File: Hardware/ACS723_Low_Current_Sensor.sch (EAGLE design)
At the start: 26 parts, among them U1 ACS723, U2 OPA344

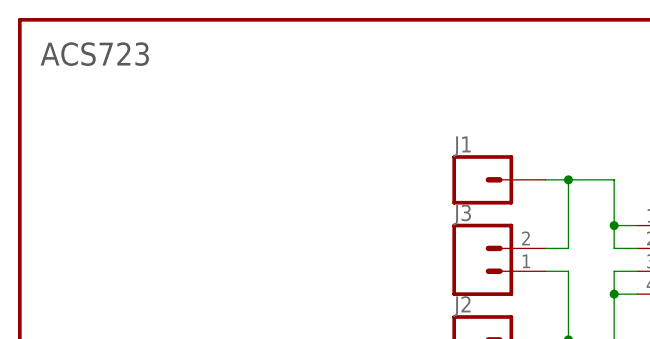
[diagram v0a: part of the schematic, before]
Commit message: SCH changes
-added full IC name
-moved some notes around
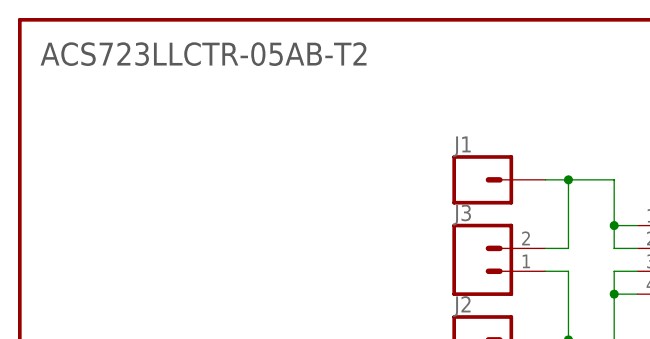
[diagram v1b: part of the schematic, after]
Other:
- note added: "ACS723LLCTR-05AB-T2"
- note removed: "ACS723"
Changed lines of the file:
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@@
 clockwise to increase
 output reference voltage</text>
-<text x="2.286" y="180.34" size="2.54" layer="97">ACS723</text>
+<text x="2.286" y="180.34" size="2.54" layer="97">ACS723LLCTR-05AB-T2</text>
 </plain>
 <instances>

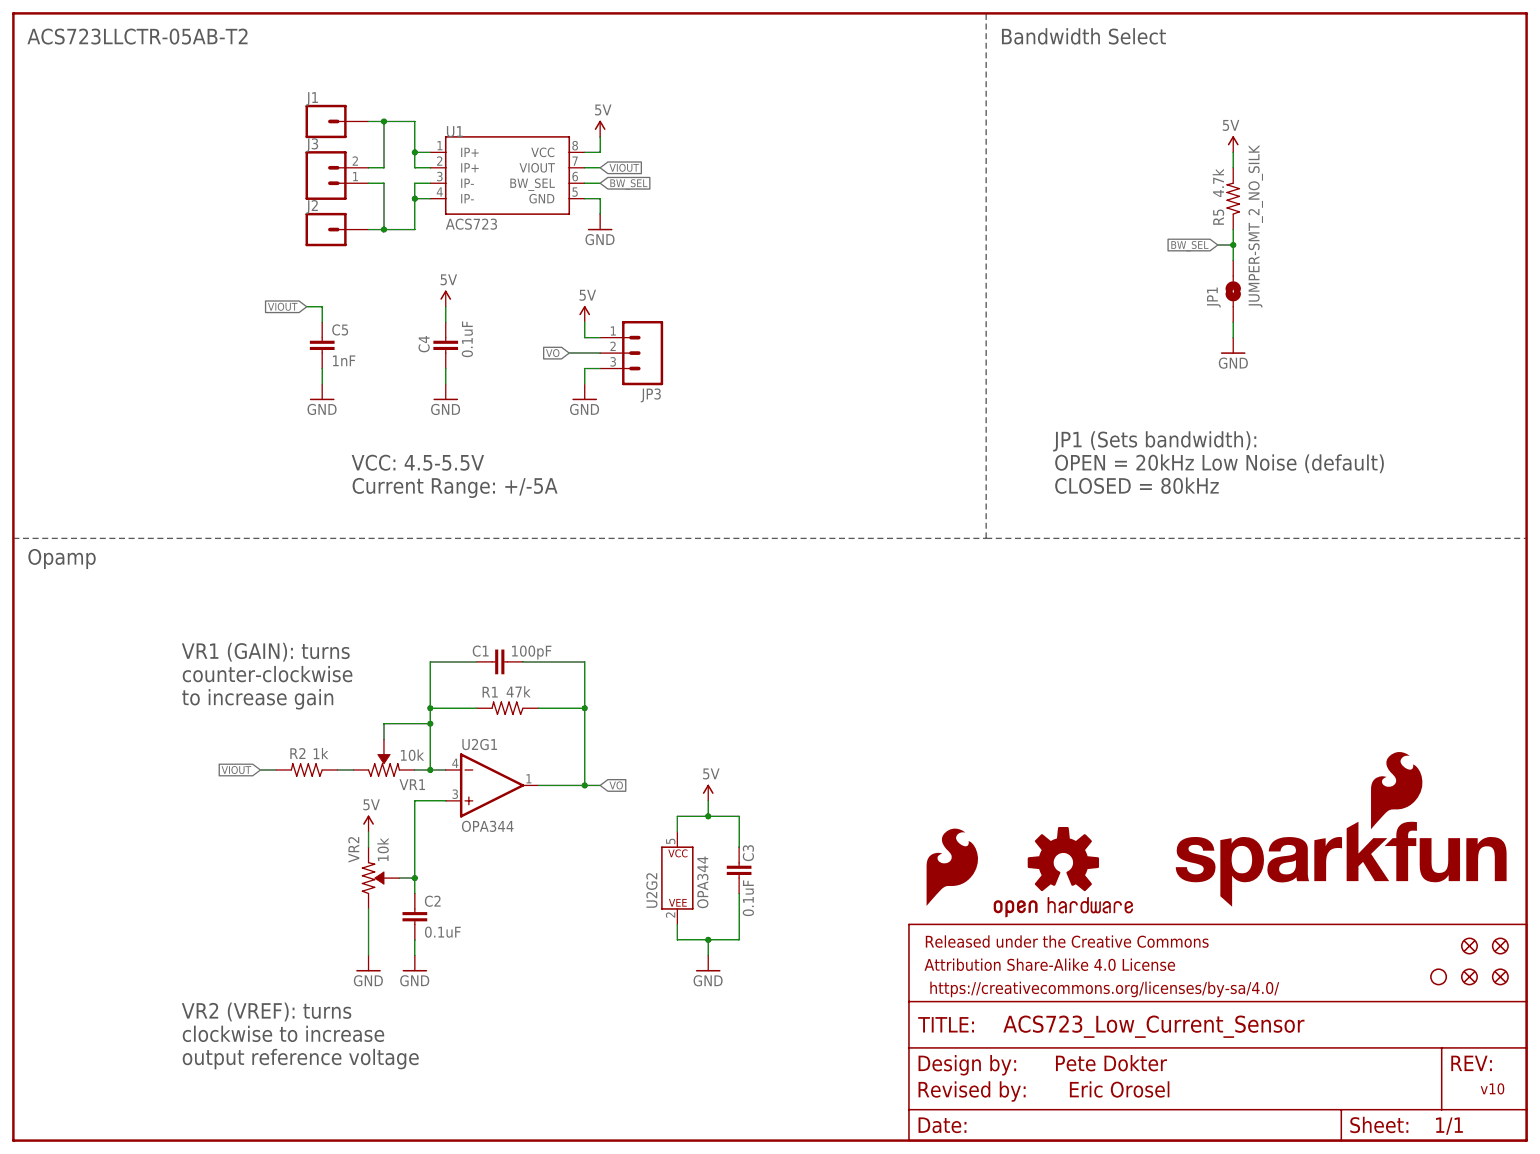
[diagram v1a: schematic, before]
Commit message: v10 finalization
-moved some vias for better GND stitching
-slight silk adjustment
-changed value of opamp voltage split to allow for similiar spectrum measurment as the previous version. With an output of 220mV more per amp the values of the gain resistors needed to be adjusted to account for this difference
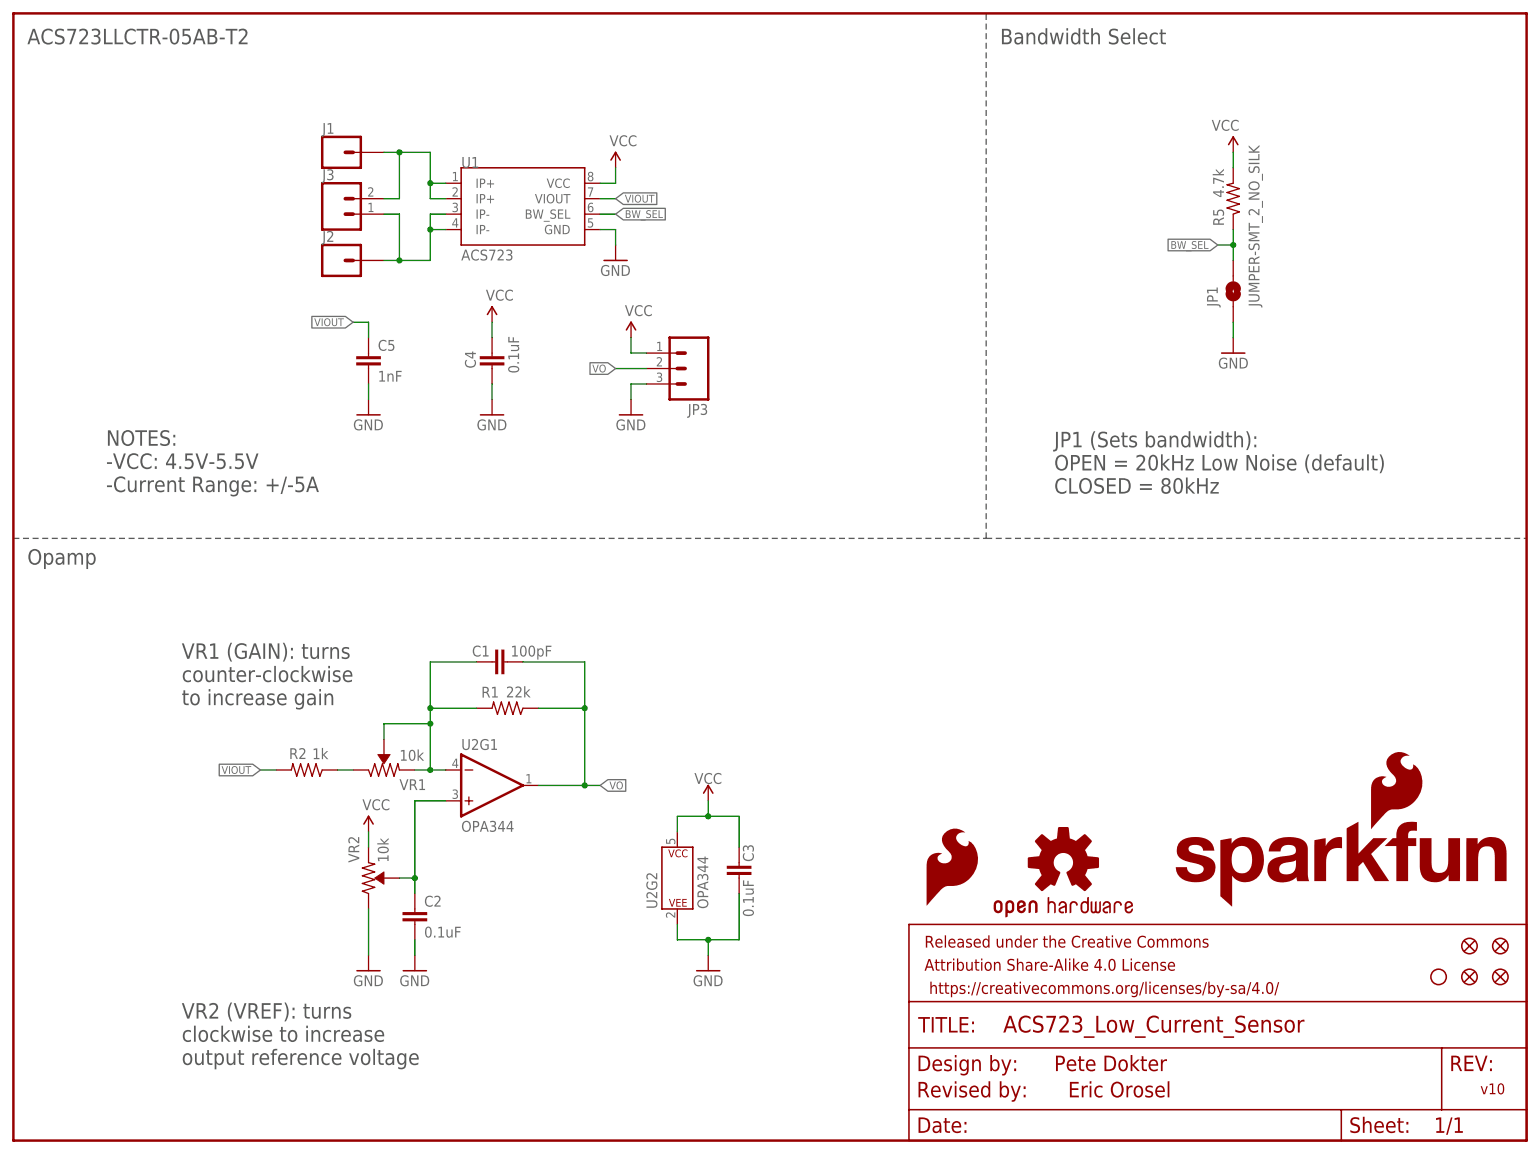
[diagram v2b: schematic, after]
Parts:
- R1: value 47k -> 22k; device SparkFun-Resistors:47KOHM-0603-1/10W-1% -> SparkFun-Resistors:22KOHM-0603-1/10W-1%
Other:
- note added: "-Current Range: +/-5A"
- note added: "-VCC: 4.5V-5.5V"
- note added: "NOTES:"
- note removed: "Current Range: +/-5A"
- note removed: "VCC: 4.5-5.5V"
- moved on the sheet: C4, C5, J1, J2, J3, JP3, U1

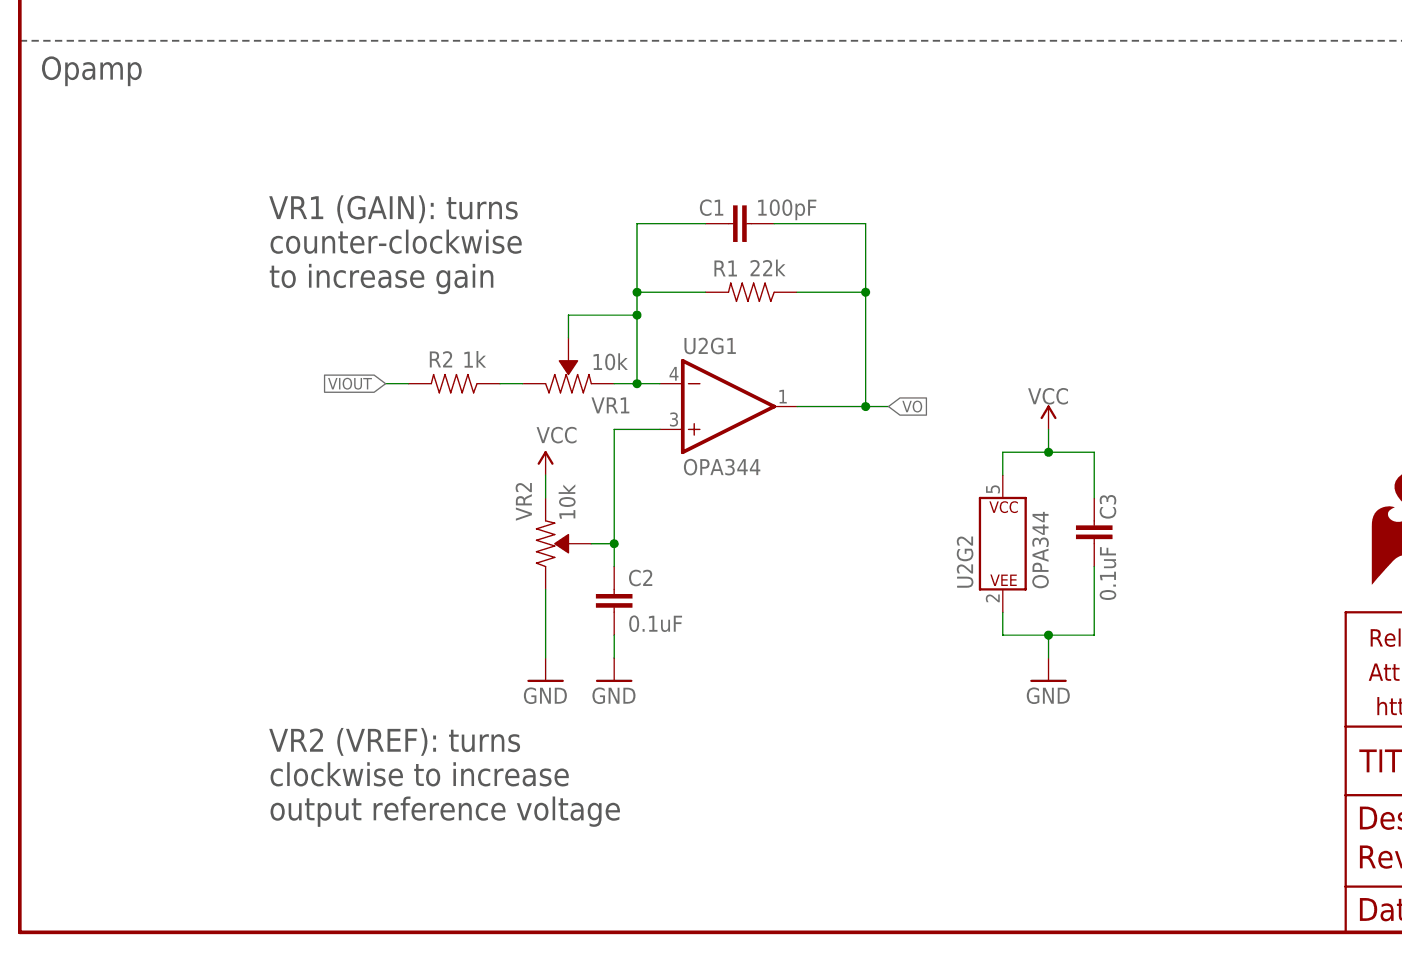
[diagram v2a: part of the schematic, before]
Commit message: post eng. checklist changes
-added notes about gain
-removed uneeded layers
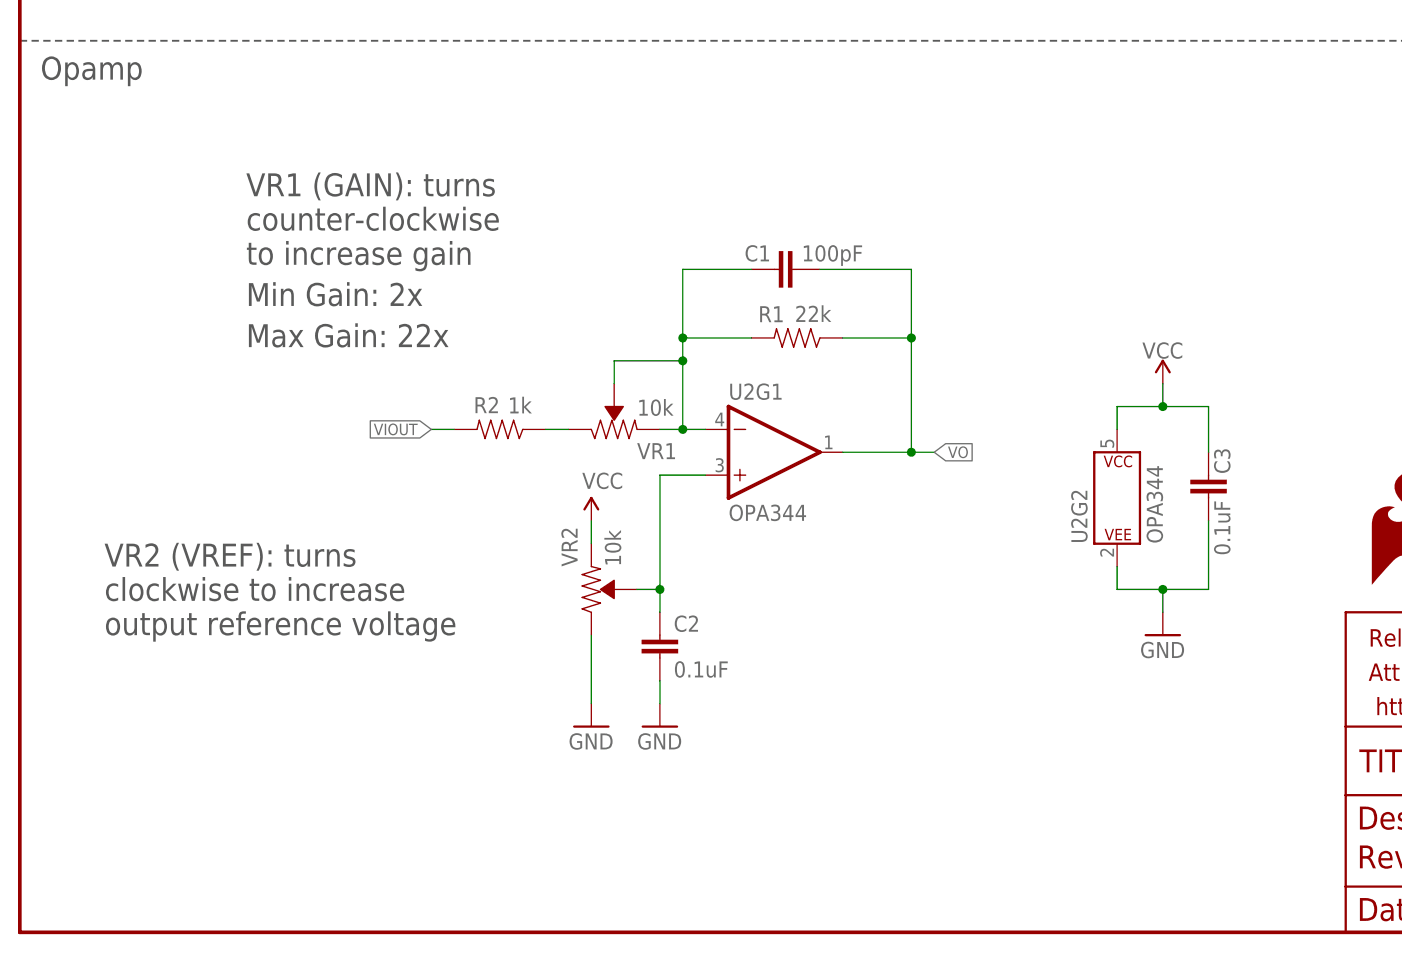
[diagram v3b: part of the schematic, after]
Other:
- note added: "Max Gain: 22x"
- note added: "Min Gain: 2x"
- moved on the sheet: C1, C2, C3, R1, R2, U2G1, U2G2, VR1, VR2
